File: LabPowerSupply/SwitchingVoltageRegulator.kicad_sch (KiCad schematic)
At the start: 14 parts

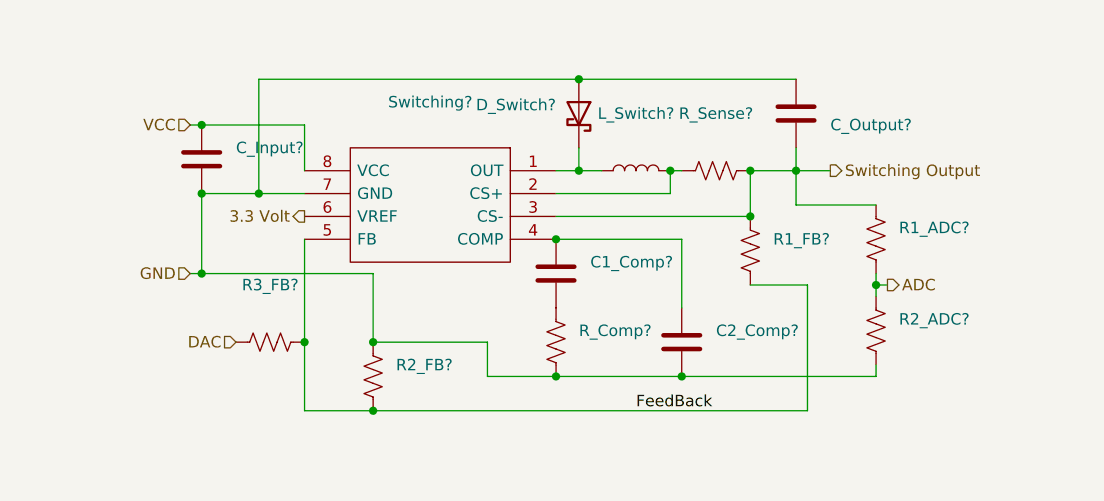
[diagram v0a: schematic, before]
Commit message: Finished first pass on the schematic
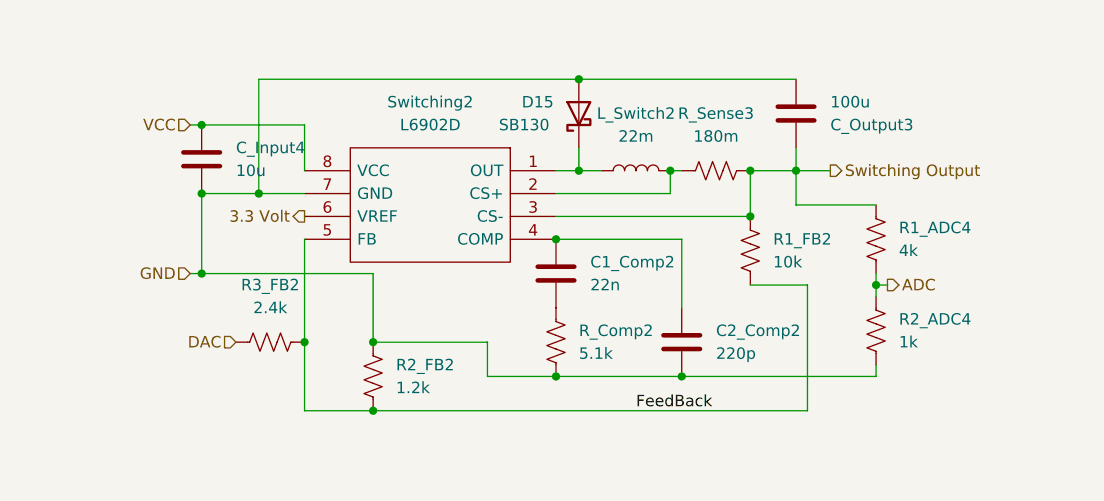
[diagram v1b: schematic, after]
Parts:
- removed D_Switch?: ~, symbol Diode:SB130
- added D15: SB130, Diode_THT:D_DO-41_SOD81_P10.16mm_Horizontal, symbol Diode:SB130
- C1_Comp2: renamed from C1_Comp?; value ~ -> 22n; footprint (none) -> Capacitor_SMD:C_1210_3225Metric
- C2_Comp2: renamed from C2_Comp?; value ~ -> 220p; footprint (none) -> Capacitor_SMD:C_1210_3225Metric
- C_Input4: renamed from C_Input?; value ~ -> 10u; footprint (none) -> Capacitor_SMD:C_1210_3225Metric
- C_Output3: renamed from C_Output?; value ~ -> 100u; footprint (none) -> Capacitor_SMD:C_1210_3225Metric
- L_Switch2: renamed from L_Switch?; value ~ -> 22m; footprint (none) -> Inductor_THT:L_Radial_D8.7mm_P5.00mm_Fastron_07HCP
- R1_ADC4: renamed from R1_ADC?; value ~ -> 4k; footprint (none) -> Resistor_SMD:R_1210_3225Metric
- R1_FB2: renamed from R1_FB?; value ~ -> 10k; footprint (none) -> Resistor_SMD:R_1210_3225Metric
- R2_ADC4: renamed from R2_ADC?; value ~ -> 1k; footprint (none) -> Resistor_SMD:R_1210_3225Metric
- R2_FB2: renamed from R2_FB?; value ~ -> 1.2k; footprint (none) -> Resistor_SMD:R_1210_3225Metric
- R3_FB2: renamed from R3_FB?; value ~ -> 2.4k; footprint (none) -> Resistor_SMD:R_1210_3225Metric
- R_Comp2: renamed from R_Comp?; value ~ -> 5.1k; footprint (none) -> Resistor_SMD:R_1210_3225Metric
- R_Sense3: renamed from R_Sense?; value ~ -> 180m; footprint (none) -> Resistor_SMD:R_1210_3225Metric
- Switching2: renamed from Switching?; value ~ -> L6902D
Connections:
- net GND: now also D15.2 (A)
- net at L_Switch2.1, Switching2.1 (OUT): now also D15.1 (K)

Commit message: started PCB
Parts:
- L_Switch2: footprint Inductor_THT:L_Radial_D8.7mm_P5.00mm_Fastron_07HCP -> Inductor_THT:L_Radial_D6.0mm_P4.00mm
- Switching2: footprint (none) -> Package_SO:SOIC-8-1EP_3.9x4.9mm_P1.27mm_EP2.95x4.9mm_Mask2.71x3.4mm
- renumbered C_Input4 to C_Input3
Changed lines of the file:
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@@
     (property "Reference" "Switching2" (id 0) (at 124.46 85.09 0))
     (property "Value" "L6902D" (id 1) (at 124.46 87.63 0))
-    (property "Footprint" "" (id 2) (at 114.3 90.17 0)
+    (property "Footprint" "Package_SO:SOIC-8-1EP_3.9x4.9mm_P1.27mm_EP2.95x4.9mm_Mask2.71x3.4mm" (id 2) (at 114.3 90.17 0)
       (effects (font (size 1.27 1.27)) (justify left) hide)
     )
@@
     (property "Reference" "L_Switch2" (id 0) (at 147.32 86.36 90))
     (property "Value" "22m" (id 1) (at 147.32 88.9 90))
-    (property "Footprint" "Inductor_THT:L_Radial_D8.7mm_P5.00mm_Fastron_07HCP" (id 2) (at 147.32 92.71 0)
+    (property "Footprint" "Inductor_THT:L_Radial_D6.0mm_P4.00mm" (id 2) (at 147.32 92.71 0)
       (effects (font (size 1.27 1.27)) hide)
     )
@@
   (symbol (lib_id "Device:C") (at 99.06 91.44 0) (unit 1)
     (in_bom yes) (on_board yes) (fields_autoplaced)
-    (property "Reference" "C_Input4" (id 0) (at 102.87 90.1699 0)
+    (property "Reference" "C_Input3" (id 0) (at 102.87 90.1699 0)
       (effects (font (size 1.27 1.27)) (justify left))
     )

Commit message: more work
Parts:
- renumbered C_Input3 to C1_SVR1, C_Output3 to C2_SVR1, C1_Comp2 to C3_SVR1, C2_Comp2 to C4_SVR1, D15 to D_SVR1, L_Switch2 to L_SVR1, R_Sense3 to R1_SVR1, R1_FB2 to R2_SVR1, R1_ADC4 to R3_SVR1, R3_FB2 to R4_SVR1, R_Comp2 to R5_SVR1, R2_ADC4 to R6_SVR1, R2_FB2 to R7_SVR1, Switching2 to Switching1
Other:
- moved on the sheet: C1_SVR1, C2_SVR1, C4_SVR1, D_SVR1, R1_SVR1, R2_SVR1, R3_SVR1, R4_SVR1, R6_SVR1, R7_SVR1

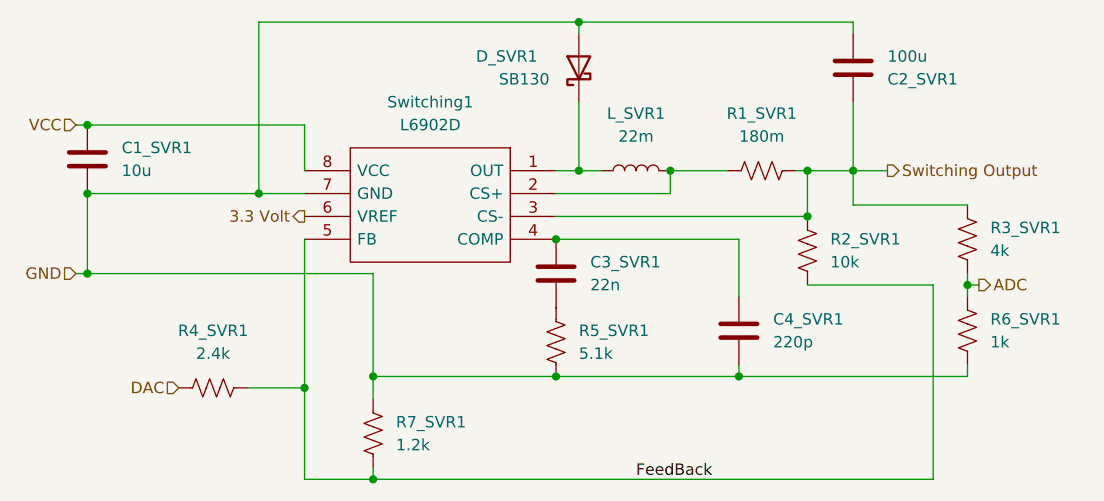
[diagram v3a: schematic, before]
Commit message: Resistor footprints changed to 0603
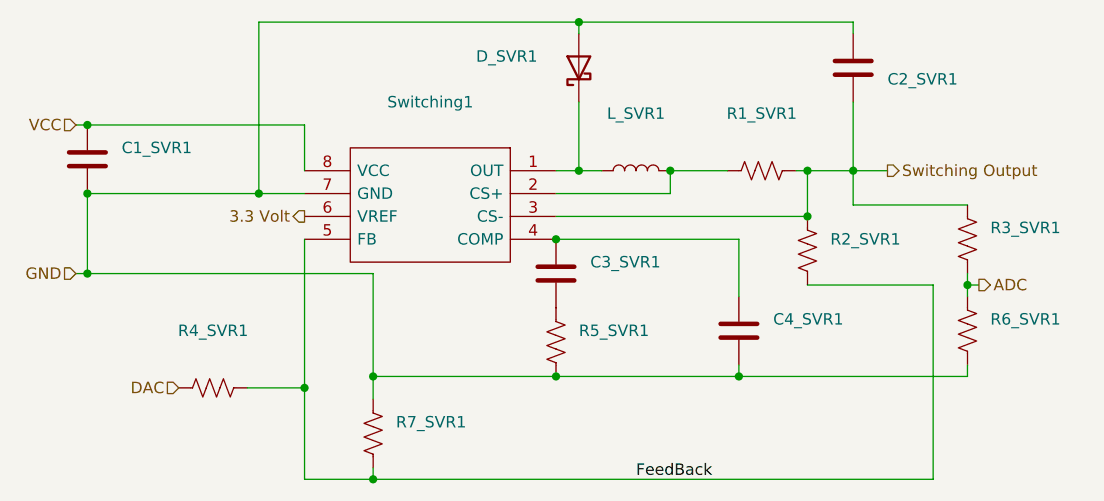
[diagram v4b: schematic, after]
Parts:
- C1_SVR1: value 10u -> (none); footprint Capacitor_SMD:C_1210_3225Metric -> (none)
- C2_SVR1: value 100u -> (none); footprint Capacitor_SMD:C_1210_3225Metric -> (none)
- C3_SVR1: value 22n -> (none); footprint Capacitor_SMD:C_1210_3225Metric -> (none)
- C4_SVR1: value 220p -> (none); footprint Capacitor_SMD:C_1210_3225Metric -> (none)
- D_SVR1: value SB130 -> (none); footprint Diode_THT:D_DO-41_SOD81_P10.16mm_Horizontal -> (none)
- L_SVR1: value 22m -> (none); footprint Inductor_THT:L_Radial_D6.0mm_P4.00mm -> (none)
- R1_SVR1: value 180m -> (none); footprint Resistor_SMD:R_1210_3225Metric -> (none)
- R2_SVR1: value 10k -> (none); footprint Resistor_SMD:R_1210_3225Metric -> (none)
- R3_SVR1: value 4k -> (none); footprint Resistor_SMD:R_1210_3225Metric -> (none)
- R4_SVR1: value 2.4k -> (none); footprint Resistor_SMD:R_1210_3225Metric -> (none)
- R5_SVR1: value 5.1k -> (none); footprint Resistor_SMD:R_1210_3225Metric -> (none)
- R6_SVR1: value 1k -> (none); footprint Resistor_SMD:R_1210_3225Metric -> (none)
- R7_SVR1: value 1.2k -> (none); footprint Resistor_SMD:R_1210_3225Metric -> (none)
- Switching1: value L6902D -> (none); footprint Package_SO:SOIC-8-1EP_3.9x4.9mm_P1.27mm_EP2.95x4.9mm_Mask2.71x3.4mm -> (none)
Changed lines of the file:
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@@
       (effects (font (size 1.27 1.27)) (justify left))
     )
-    (property "Value" "1.2k" (id 1) (at 120.65 123.1899 0)
-      (effects (font (size 1.27 1.27)) (justify left))
-    )
-    (property "Footprint" "Resistor_SMD:R_1210_3225Metric" (id 2) (at 119.126 122.174 90)
+    (property "Value" "" (id 1) (at 120.65 123.1899 0)
+      (effects (font (size 1.27 1.27)) (justify left))
+    )
+    (property "Footprint" "" (id 2) (at 119.126 122.174 90)
       (effects (font (size 1.27 1.27)) hide)
     )
@@
     (in_bom yes) (on_board yes) (fields_autoplaced)
     (property "Reference" "R1_SVR1" (id 0) (at 161.29 86.36 90))
-    (property "Value" "180m" (id 1) (at 161.29 88.9 90))
-    (property "Footprint" "Resistor_SMD:R_1210_3225Metric" (id 2) (at 161.544 91.694 90)
+    (property "Value" "" (id 1) (at 161.29 88.9 90))
+    (property "Footprint" "" (id 2) (at 161.544 91.694 90)
       (effects (font (size 1.27 1.27)) hide)
     )
@@
       (effects (font (size 1.27 1.27)) (justify right))
     )
-    (property "Value" "SB130" (id 1) (at 132.08 82.55 90)
+    (property "Value" "" (id 1) (at 132.08 82.55 90)
       (effects (font (size 1.27 1.27)) (justify right))
     )
-    (property "Footprint" "Diode_THT:D_DO-41_SOD81_P10.16mm_Horizontal" (id 2) (at 145.415 81.28 0)
+    (property "Footprint" "" (id 2) (at 145.415 81.28 0)
       (effects (font (size 1.27 1.27)) hide)
     )
@@
       (effects (font (size 1.27 1.27)) (justify left))
     )
-    (property "Value" "22n" (id 1) (at 142.24 105.4099 0)
-      (effects (font (size 1.27 1.27)) (justify left))
-    )
-    (property "Footprint" "Capacitor_SMD:C_1210_3225Metric" (id 2) (at 139.3952 107.95 0)
+    (property "Value" "" (id 1) (at 142.24 105.4099 0)
+      (effects (font (size 1.27 1.27)) (justify left))
+    )
+    (property "Footprint" "" (id 2) (at 139.3952 107.95 0)
       (effects (font (size 1.27 1.27)) hide)
     )
@@
     (in_bom yes) (on_board yes) (fields_autoplaced)
     (property "Reference" "Switching1" (id 0) (at 124.46 85.09 0))
-    (property "Value" "L6902D" (id 1) (at 124.46 87.63 0))
-    (property "Footprint" "Package_SO:SOIC-8-1EP_3.9x4.9mm_P1.27mm_EP2.95x4.9mm_Mask2.71x3.4mm" (id 2) (at 114.3 90.17 0)
+    (property "Value" "" (id 1) (at 124.46 87.63 0))
+    (property "Footprint" "" (id 2) (at 114.3 90.17 0)
       (effects (font (size 1.27 1.27)) (justify left) hide)
     )
@@
     (in_bom yes) (on_board yes) (fields_autoplaced)
     (property "Reference" "L_SVR1" (id 0) (at 147.32 86.36 90))
-    (property "Value" "22m" (id 1) (at 147.32 88.9 90))
-    (property "Footprint" "Inductor_THT:L_Radial_D6.0mm_P4.00mm" (id 2) (at 147.32 92.71 0)
+    (property "Value" "" (id 1) (at 147.32 88.9 90))
+    (property "Footprint" "" (id 2) (at 147.32 92.71 0)
       (effects (font (size 1.27 1.27)) hide)
     )
@@
     (in_bom yes) (on_board yes) (fields_autoplaced)
     (property "Reference" "R4_SVR1" (id 0) (at 100.33 110.49 90))
-    (property "Value" "2.4k" (id 1) (at 100.33 113.03 90))
-    (property "Footprint" "Resistor_SMD:R_1210_3225Metric" (id 2) (at 100.076 117.856 90)
+    (property "Value" "" (id 1) (at 100.33 113.03 90))
+    (property "Footprint" "" (id 2) (at 100.076 117.856 90)
       (effects (font (size 1.27 1.27)) hide)
     )
@@
       (effects (font (size 1.27 1.27)) (justify left))
     )
-    (property "Value" "1k" (id 1) (at 186.69 111.7599 0)
-      (effects (font (size 1.27 1.27)) (justify left))
-    )
-    (property "Footprint" "Resistor_SMD:R_1210_3225Metric" (id 2) (at 185.166 110.744 90)
+    (property "Value" "" (id 1) (at 186.69 111.7599 0)
+      (effects (font (size 1.27 1.27)) (justify left))
+    )
+    (property "Footprint" "" (id 2) (at 185.166 110.744 90)
       (effects (font (size 1.27 1.27)) hide)
     )
@@
       (effects (font (size 1.27 1.27)) (justify left))
     )
-    (property "Value" "10u" (id 1) (at 90.17 92.7099 0)
-      (effects (font (size 1.27 1.27)) (justify left))
-    )
-    (property "Footprint" "Capacitor_SMD:C_1210_3225Metric" (id 2) (at 87.3252 95.25 0)
+    (property "Value" "" (id 1) (at 90.17 92.7099 0)
+      (effects (font (size 1.27 1.27)) (justify left))
+    )
+    (property "Footprint" "" (id 2) (at 87.3252 95.25 0)
       (effects (font (size 1.27 1.27)) hide)
     )
@@
       (effects (font (size 1.27 1.27)) (justify left))
     )
-    (property "Value" "100u" (id 1) (at 175.26 80.0101 0)
-      (effects (font (size 1.27 1.27)) (justify left))
-    )
-    (property "Footprint" "Capacitor_SMD:C_1210_3225Metric" (id 2) (at 172.4152 77.47 0)
+    (property "Value" "" (id 1) (at 175.26 80.0101 0)
+      (effects (font (size 1.27 1.27)) (justify left))
+    )
+    (property "Footprint" "" (id 2) (at 172.4152 77.47 0)
       (effects (font (size 1.27 1.27)) hide)
     )
@@
       (effects (font (size 1.27 1.27)) (justify left))
     )
-    (property "Value" "4k" (id 1) (at 186.69 101.5999 0)
-      (effects (font (size 1.27 1.27)) (justify left))
-    )
-    (property "Footprint" "Resistor_SMD:R_1210_3225Metric" (id 2) (at 185.166 100.584 90)
+    (property "Value" "" (id 1) (at 186.69 101.5999 0)
+      (effects (font (size 1.27 1.27)) (justify left))
+    )
+    (property "Footprint" "" (id 2) (at 185.166 100.584 90)
       (effects (font (size 1.27 1.27)) hide)
     )
@@
       (effects (font (size 1.27 1.27)) (justify left))
     )
-    (property "Value" "220p" (id 1) (at 162.56 111.7599 0)
-      (effects (font (size 1.27 1.27)) (justify left))
-    )
-    (property "Footprint" "Capacitor_SMD:C_1210_3225Metric" (id 2) (at 159.7152 114.3 0)
+    (property "Value" "" (id 1) (at 162.56 111.7599 0)
+      (effects (font (size 1.27 1.27)) (justify left))
+    )
+    (property "Footprint" "" (id 2) (at 159.7152 114.3 0)
       (effects (font (size 1.27 1.27)) hide)
     )
@@
       (effects (font (size 1.27 1.27)) (justify left))
     )
-    (property "Value" "10k" (id 1) (at 168.91 102.8699 0)
-      (effects (font (size 1.27 1.27)) (justify left))
-    )
-    (property "Footprint" "Resistor_SMD:R_1210_3225Metric" (id 2) (at 167.386 101.854 90)
+    (property "Value" "" (id 1) (at 168.91 102.8699 0)
+      (effects (font (size 1.27 1.27)) (justify left))
+    )
+    (property "Footprint" "" (id 2) (at 167.386 101.854 90)
       (effects (font (size 1.27 1.27)) hide)
     )
@@
       (effects (font (size 1.27 1.27)) (justify left))
     )
-    (property "Value" "5.1k" (id 1) (at 140.97 113.0299 0)
-      (effects (font (size 1.27 1.27)) (justify left))
-    )
-    (property "Footprint" "Resistor_SMD:R_1210_3225Metric" (id 2) (at 139.446 112.014 90)
-      (effects (font (size 1.27 1.27)) hide)
-    )
+    (property "Value" "" (id 1) (at 140.97 113.0299 0)
+      (effects (font (size 1.27 1.27)) (justify left))
+    )
+    (property "Footprint" "" (id 2) (at 139.446 112.014 90)
+      (effects (font (size 1.27 1.27)) hide)
+    )
